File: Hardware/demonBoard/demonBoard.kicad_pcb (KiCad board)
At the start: 6 copper layers, 60 x 90 mm, 108 parts, among them J1 TYPE-C-31-M-12, J10 MOTOR_RIGHT_CONN, J2 UART_CONN, J3 LED_LEFT_CONN, J4 LED_TAIL_CONN, J5 LED_RIGHT_CONN, J6 BATT_CONN, J7 LED_AUX1_CONN, J8 LED_AUX2_CONN, J9 MOTOR_LEFT_CONN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

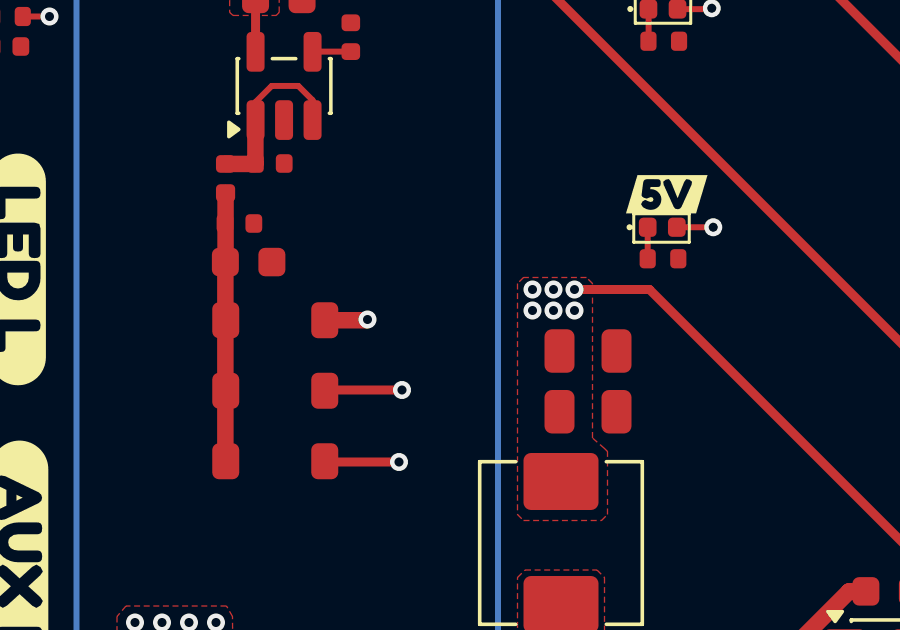
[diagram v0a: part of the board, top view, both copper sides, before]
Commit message: fix: Fix 5V connection
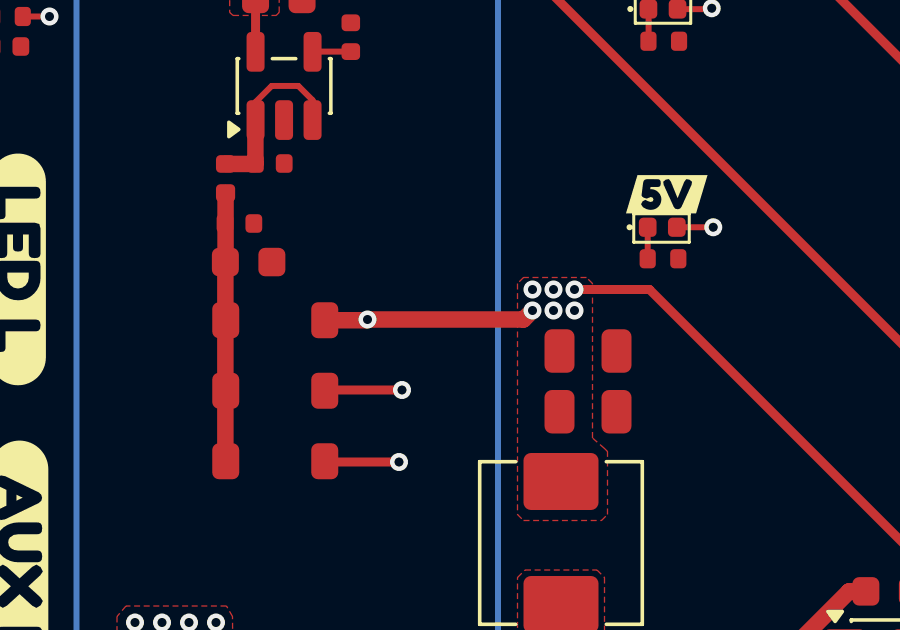
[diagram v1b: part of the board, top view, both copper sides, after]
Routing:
- net +5V: track 83.5 -> 89.1 mm
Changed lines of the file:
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@@
+	)
+	(segment
+		(start 136.64 84.85)
+		(end 141.84 84.85)
+		(width 0.55)
+		(layer "F.Cu")
+		(net 55)
 	)
 	(segment
@@
 		(layer "F.Cu")
 		(net 55)
+	)
+	(segment
+		(start 141.84 84.85)
+		(end 142.14 84.55)
+		(width 0.55)
+		(layer "F.Cu")
+		(net 55)

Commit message: Change resistors for leds
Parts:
- C16, C17: value 22u -> 22u/25V
- C19: value 47n -> 470p
- C20: value 68p -> 8.7p
- R12: value 22.1k -> 82k
- R15, R20: value 1k -> 10k
- R3: value 110R -> 10k
- R8, R9: value 0R -> 22R
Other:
- board text added: "Trace missing, must solder external wire"
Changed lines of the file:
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@@
 			)
 		)
-		(property "Value" "1k"
+		(property "Value" "10k"
 			(at 0 1.17 0)
 			(layer "F.Fab")
@@
 			)
 		)
-		(property "Value" "22u"
+		(property "Value" "22u/25V"
 			(at 0 1.68 90)
 			(layer "F.Fab")
@@
 			)
 		)
-		(property "Value" "0R"
+		(property "Value" "22R"
 			(at 0 1.17 180)
 			(layer "F.Fab")
@@
 			)
 		)
-		(property "Value" "110R"
+		(property "Value" "10k"
 			(at 0 1.17 0)
 			(layer "F.Fab")
@@
 			)
 		)
-		(property "Value" "22u"
+		(property "Value" "22u/25V"
 			(at 0 1.68 90)
 			(layer "F.Fab")
@@
 			)
 		)
-		(property "Value" "1k"
+		(property "Value" "10k"
 			(at 0 1.17 0)
 			(layer "F.Fab")
@@
 			)
 		)
-		(property "Value" "47n"
+		(property "Value" "470p"
 			(at 0 1.16 90)
 			(layer "F.Fab")
@@
 			)
 		)
-		(property "Value" "68p"
+		(property "Value" "8.7p"
 			(at 0 1.16 90)
 			(layer "F.Fab")
@@
 		(sheetname "/Voltage regulators and voltage sense/")
 		(sheetfile "voltage_regulators_and_voltage_sense.kicad_sch")
-		(attr smd)
+		(attr smd dnp)
 		(fp_line
 			(start 0.91 -0.46)
@@
 		(sheetname "/Voltage regulators and voltage sense/")
 		(sheetfile "voltage_regulators_and_voltage_sense.kicad_sch")
-		(attr smd dnp)
+		(attr smd)
 		(fp_line
 			(start 3.41 -3.41)
@@
 			)
 		)
-		(property "Value" "0R"
+		(property "Value" "22R"
 			(at 0 1.17 180)
 			(layer "F.Fab")
@@
 			)
 		)
-		(property "Value" "22.1k"
+		(property "Value" "82k"
 			(at 0 1.17 270)
 			(layer "F.Fab")
@@
 	)
 	(gr_line
+		(start 111.115 64.475)
+		(end 137.89 84.725)
+		(stroke
+			(width 0.3)
+			(type solid)
+		)
+		(layer "Dwgs.User")
+	)
+	(gr_line
+		(start 137.89 84.775)
+		(end 137.015 84.775)
+		(stroke
+			(width 0.3)
+			(type solid)
+		)
+		(layer "Dwgs.User")
+	)
+	(gr_line
+		(start 137.89 84.7)
+		(end 137.89 83.95)
+		(stroke
+			(width 0.3)
+			(type solid)
+		)
+		(layer "Dwgs.User")
+	)
+	(gr_line
 		(start 115.49 143.2)
 		(end 115.49 63.2)
@@
 		(layer "Edge.Cuts")
 	)
+	(gr_text "Trace missing,\nmust solder external wire"
+		(at 93.565 63.85 0)
+		(layer "Dwgs.User")
+		(effects
+			(font
+				(size 1 1)
+				(thickness 0.15)
+			)
+			(justify left bottom)
+		)
+	)
 	(dimension

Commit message: Feat: Basic program
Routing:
- net +5V: track 89.1 -> 83.5 mm
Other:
- board text removed: "Trace missing, must solder external wire"
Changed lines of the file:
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@@
-	)
-	(gr_line
-		(start 111.115 64.475)
-		(end 137.89 84.725)
-		(stroke
-			(width 0.3)
-			(type solid)
-		)
-		(layer "Dwgs.User")
-	)
-	(gr_line
-		(start 137.89 84.775)
-		(end 137.015 84.775)
-		(stroke
-			(width 0.3)
-			(type solid)
-		)
-		(layer "Dwgs.User")
-	)
-	(gr_line
-		(start 137.89 84.7)
-		(end 137.89 83.95)
-		(stroke
-			(width 0.3)
-			(type solid)
-		)
-		(layer "Dwgs.User")
 	)
 	(gr_line
@@
 		(locked yes)
 		(layer "Edge.Cuts")
-	)
-	(gr_text "Trace missing,\nmust solder external wire"
-		(at 93.565 63.85 0)
-		(layer "Dwgs.User")
-		(effects
-			(font
-				(size 1 1)
-				(thickness 0.15)
-			)
-			(justify left bottom)
-		)
 	)
 	(dimension
@@
 	)
 	(segment
-		(start 136.64 84.85)
-		(end 141.84 84.85)
-		(width 0.55)
-		(layer "F.Cu")
-		(net 55)
-	)
-	(segment
 		(start 136.615 84.875)
 		(end 136.64 84.85)
@@
 		(layer "F.Cu")
 		(net 55)
-	)
-	(segment
-		(start 141.84 84.85)
-		(end 142.14 84.55)
-		(width 0.55)
-		(layer "F.Cu")
-		(net 55)
